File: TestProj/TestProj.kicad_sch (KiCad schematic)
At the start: 0 parts

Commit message: added sheets
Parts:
- added D1: LED, symbol Device:LED
- added R1: R_Small, symbol Device:R_Small
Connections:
- new net: D1.2 (A), R1.1
- new net +5V: R1.2
- new net GND: D1.1 (K)
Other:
- added sheet Digital (digital.kicad_sch)
- added sheet Digital1 (digital.kicad_sch)
- added sheet Power (untitled.kicad_sch)
- added sheet Power1 (untitled.kicad_sch)

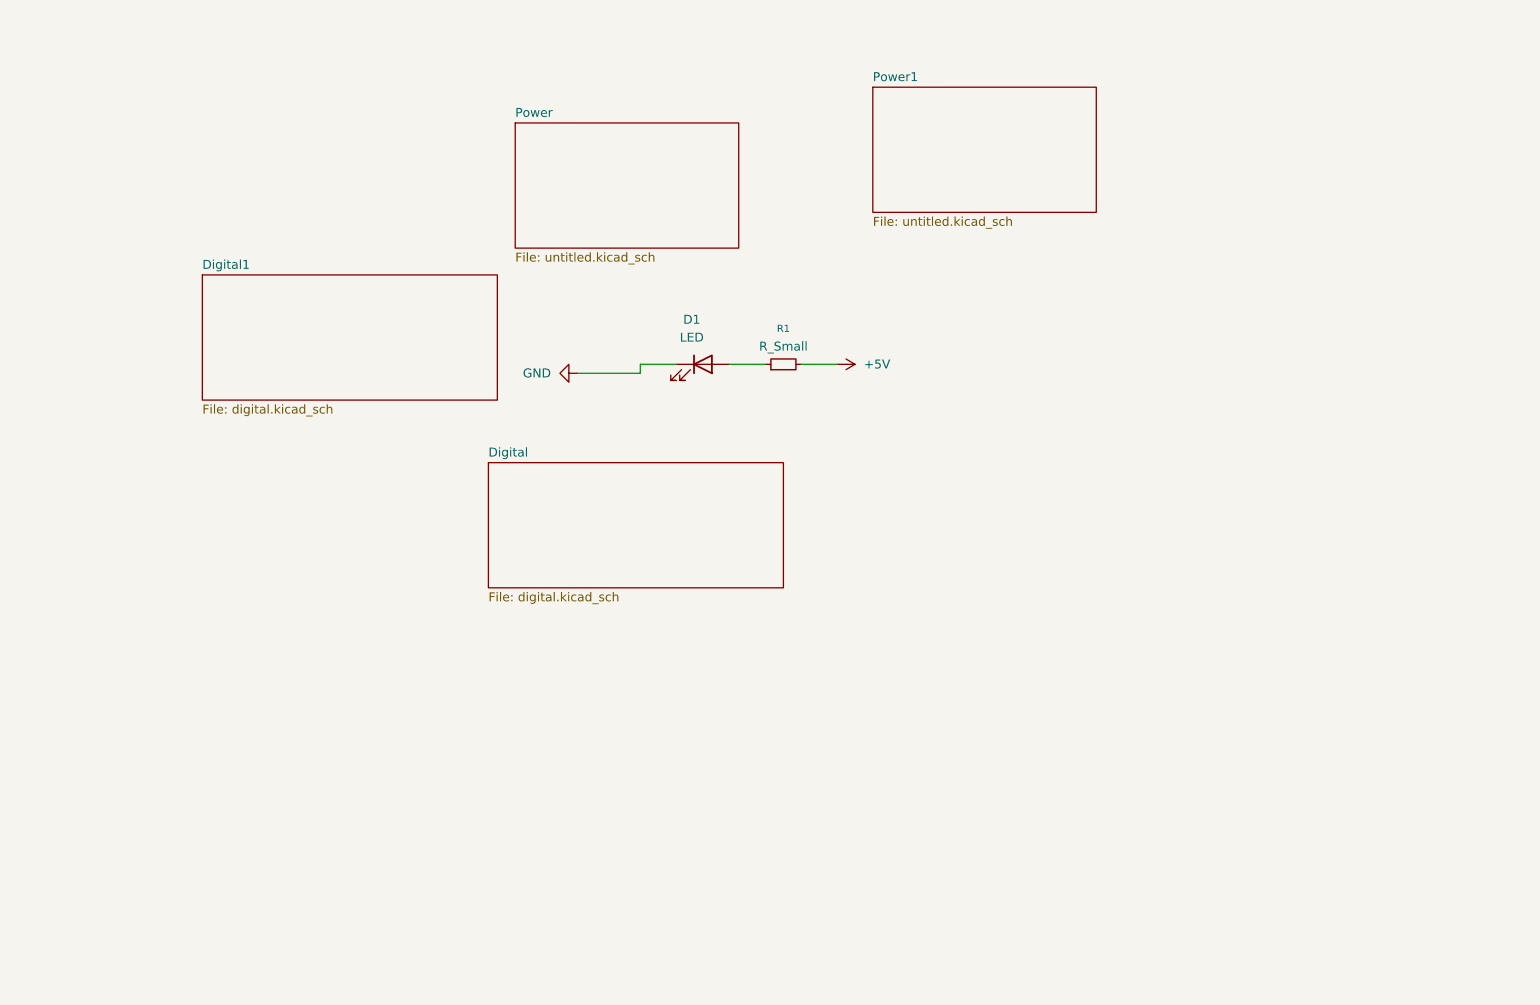
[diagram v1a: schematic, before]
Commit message: added more sheets for demonstration
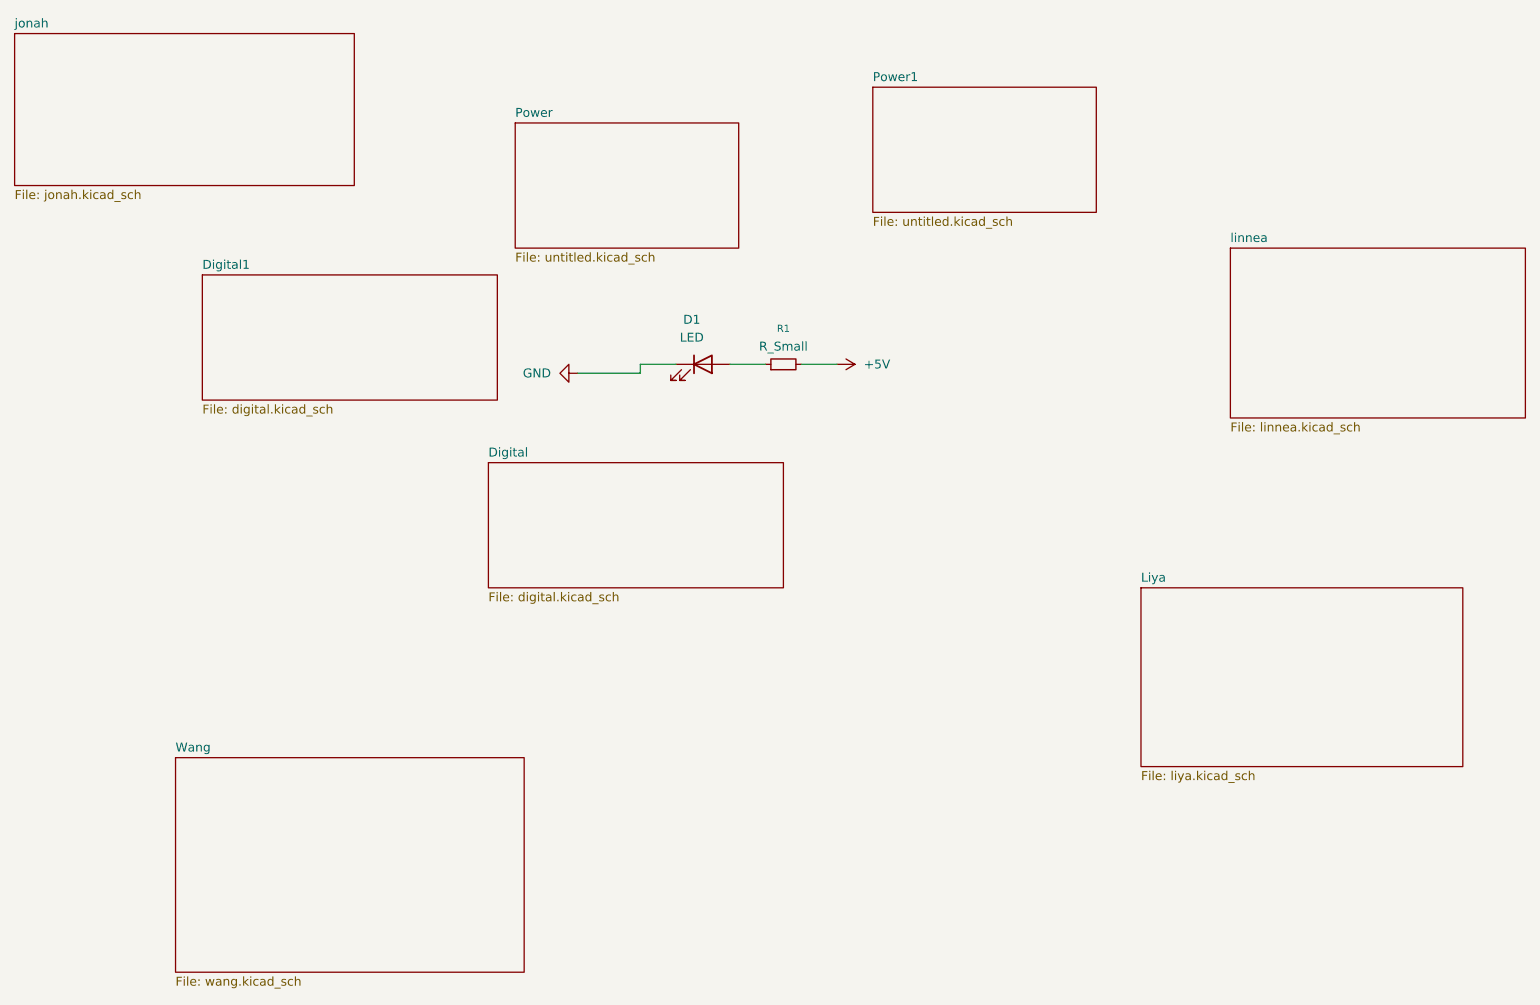
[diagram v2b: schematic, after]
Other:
- added sheet Liya (liya.kicad_sch)
- added sheet Wang (wang.kicad_sch)
- added sheet jonah (jonah.kicad_sch)
- added sheet linnea (linnea.kicad_sch)
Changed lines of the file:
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@@
+	)
+	(sheet
+		(at 43.18 36.83)
+		(size 48.26 21.59)
+		(exclude_from_sim no)
+		(in_bom yes)
+		(on_board yes)
+		(dnp no)
+		(fields_autoplaced yes)
+		(stroke
+			(width 0.1524)
+			(type solid)
+		)
+		(fill
+			(color 0 0 0 0.0000)
+		)
+		(property "Sheetname" "jonah"
+			(at 43.18 36.1184 0)
+			(effects
+				(font
+					(size 1.27 1.27)
+				)
+				(justify left bottom)
+			)
+		)
+		(property "Sheetfile" "jonah.kicad_sch"
+			(at 43.18 59.0046 0)
+			(effects
+				(font
+					(size 1.27 1.27)
+				)
+				(justify left top)
+			)
+		)
+		(instances
+			(project "TestProj"
+				(path "/c118cc56-38ad-4e47-aa36-07d1c7ff5ecd"
+					(page "9")
+				)
+			)
+		)
+	)
+	(sheet
+		(at 203.2 115.57)
+		(size 45.72 25.4)
+		(exclude_from_sim no)
+		(in_bom yes)
+		(on_board yes)
+		(dnp no)
+		(fields_autoplaced yes)
+		(stroke
+			(width 0.1524)
+			(type solid)
+		)
+		(fill
+			(color 0 0 0 0.0000)
+		)
+		(property "Sheetname" "Liya"
+			(at 203.2 114.8584 0)
+			(effects
+				(font
+					(size 1.27 1.27)
+				)
+				(justify left bottom)
+			)
+		)
+		(property "Sheetfile" "liya.kicad_sch"
+			(at 203.2 141.5546 0)
+			(effects
+				(font
+					(size 1.27 1.27)
+				)
+				(justify left top)
+			)
+		)
+		(instances
+			(project "TestProj"
+				(path "/c118cc56-38ad-4e47-aa36-07d1c7ff5ecd"
+					(page "7")
+				)
+			)
+		)
 	)
 	(sheet
@@
 	)
 	(sheet
+		(at 66.04 139.7)
+		(size 49.53 30.48)
+		(exclude_from_sim no)
+		(in_bom yes)
+		(on_board yes)
+		(dnp no)
+		(fields_autoplaced yes)
+		(stroke
+			(width 0.1524)
+			(type solid)
+		)
+		(fill
+			(color 0 0 0 0.0000)
+		)
+		(property "Sheetname" "Wang"
+			(at 66.04 138.9884 0)
+			(effects
+				(font
+					(size 1.27 1.27)
+				)
+				(justify left bottom)
+			)
+		)
+		(property "Sheetfile" "wang.kicad_sch"
+			(at 66.04 170.7646 0)
+			(effects
+				(font
+					(size 1.27 1.27)
+				)
+				(justify left top)
+			)
+		)
+		(instances
+			(project "TestProj"
+				(path "/c118cc56-38ad-4e47-aa36-07d1c7ff5ecd"
+					(page "6")
+				)
+			)
+		)
+	)
+	(sheet
 		(at 110.49 97.79)
 		(size 41.91 17.78)
@@
 				)
 			)
+		)
+	)
+	(sheet
+		(at 215.9 67.31)
+		(size 41.91 24.13)
+		(exclude_from_sim no)
+		(in_bom yes)
+		(on_board yes)
+		(dnp no)
+		(fields_autoplaced yes)
+		(stroke
+			(width 0.1524)
+			(type solid)
+		)
+		(fill
+			(color 0 0 0 0.0000)
+		)
+		(property "Sheetname" "linnea"
+			(at 215.9 66.5984 0)
+			(effects
+				(font
+					(size 1.27 1.27)
+				)
+				(justify left bottom)
+			)
+		)
+		(property "Sheetfile" "linnea.kicad_sch"
+			(at 215.9 92.0246 0)
+			(effects
+				(font
+					(size 1.27 1.27)
+				)
+				(justify left top)
+			)
+		)
+		(instances
+			(project "TestProj"
+				(path "/c118cc56-38ad-4e47-aa36-07d1c7ff5ecd"
+					(page "8")
+				)
+			)
